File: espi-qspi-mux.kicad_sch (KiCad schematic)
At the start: 10 parts, among them J11 Tag-Connect_TC2050-IDC-NL_2x5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, U17 TS3A27518E_QFN

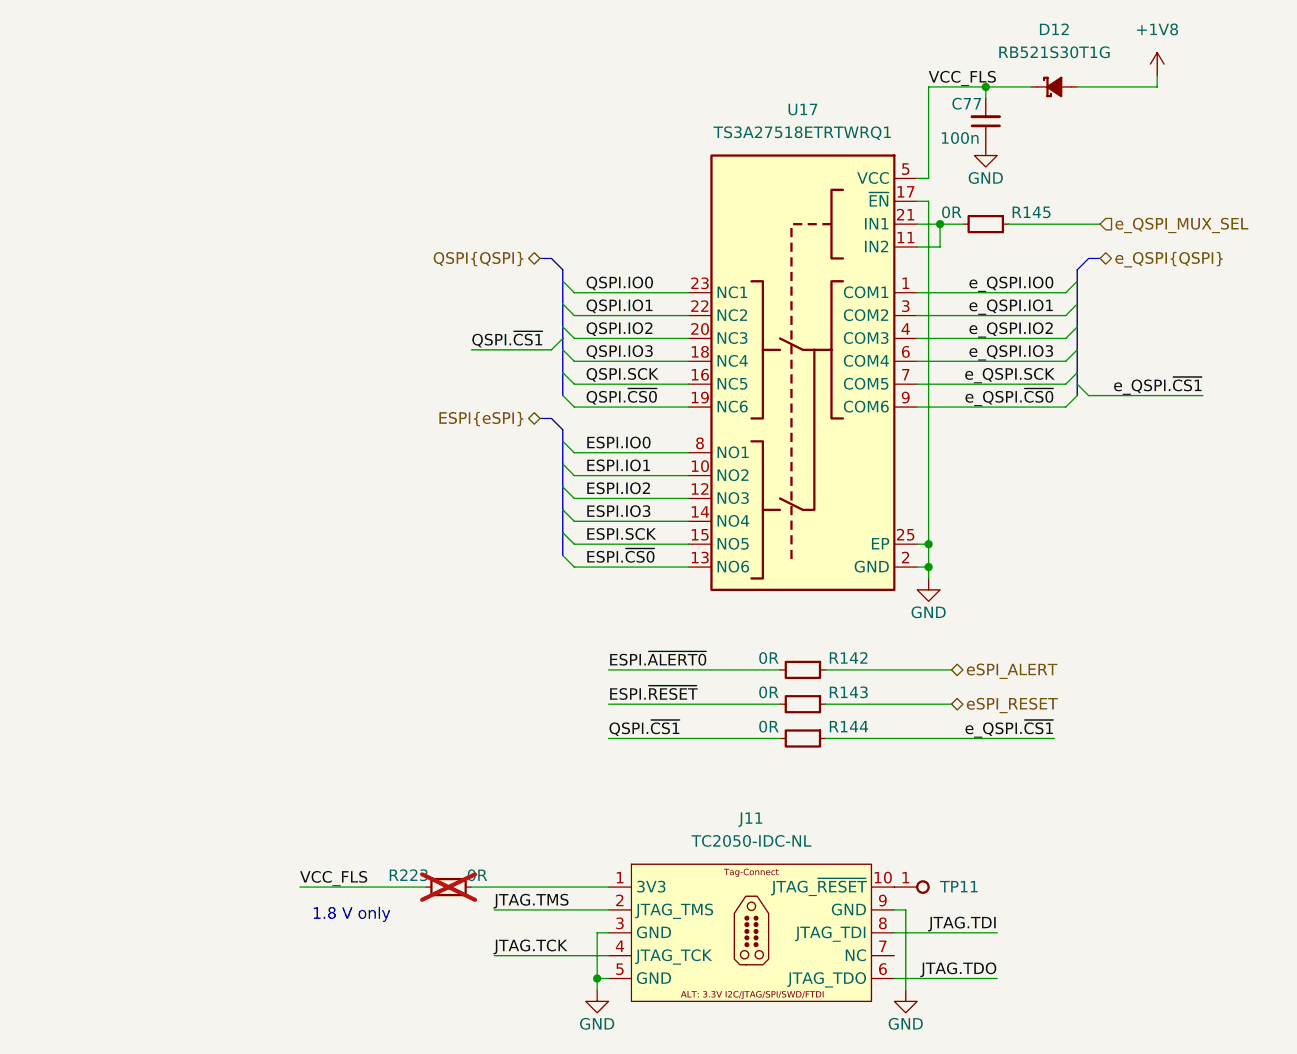
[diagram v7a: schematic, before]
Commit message: [#83652] Add ability to program BIOS SPI flash
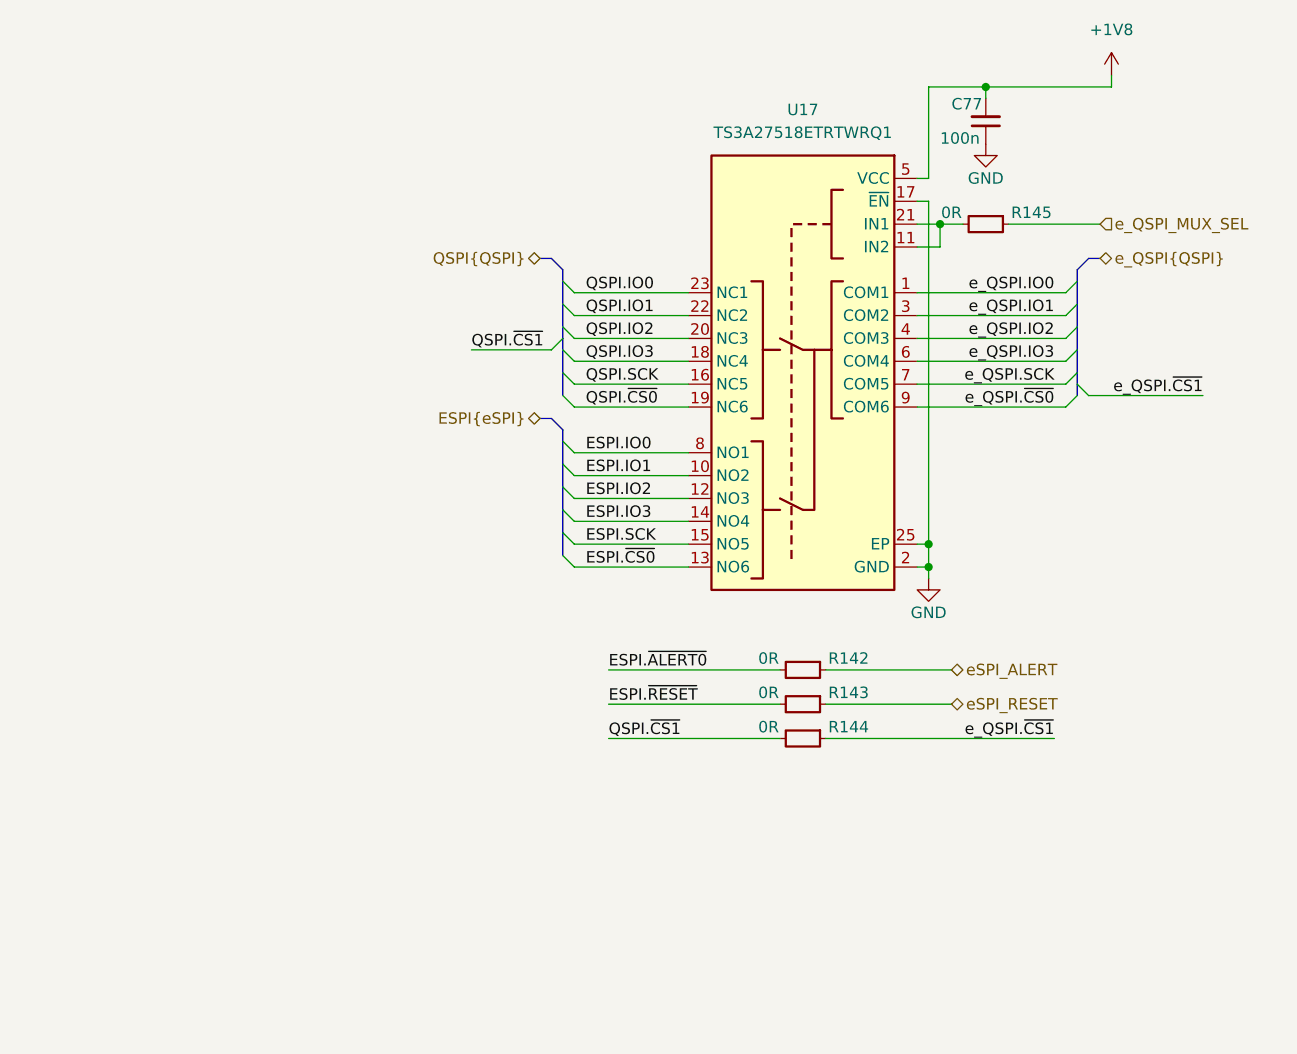
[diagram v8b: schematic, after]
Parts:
- removed D12: RB521S30T1G, antmicro-footprints:SOD-523, symbol antmicroDiodesRectifiersSingle:RB521S30T1G
- removed J11: Tag-Connect_TC2050-IDC-NL_2x5_P1.27mm, antmicro-footprints:Tag-Connect_TC2050-IDC-NL_2x5_P1.27mm, symbol antmicroTestPoints:Tag-Connect_TC2050-IDC-NL_2x5_P1.27mm
- removed R223: R_0R_0402, antmicro-footprints:R_0402_1005Metric, symbol antmicroResistors0402:R_0R_0402
- removed TP11: TP_0.75mm_SMD, antmicro-footprints:TP_SMD_0.75mm, symbol antmicroTestPoints:TP_0.75mm_SMD
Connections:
- net VCC_FLS is gone; now on net +1V8: C77.2, U17.5 (VCC)
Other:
- note removed: "1.8 V only"
